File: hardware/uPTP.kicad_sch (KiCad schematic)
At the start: 24 parts, among them J1 UART_HDR, J2 PPS_UFL, J3 PPS_SMA, J5 AUX_PWR, J6 PROG, U1 CH32V307WCU6, X1 X50328MSB2GI

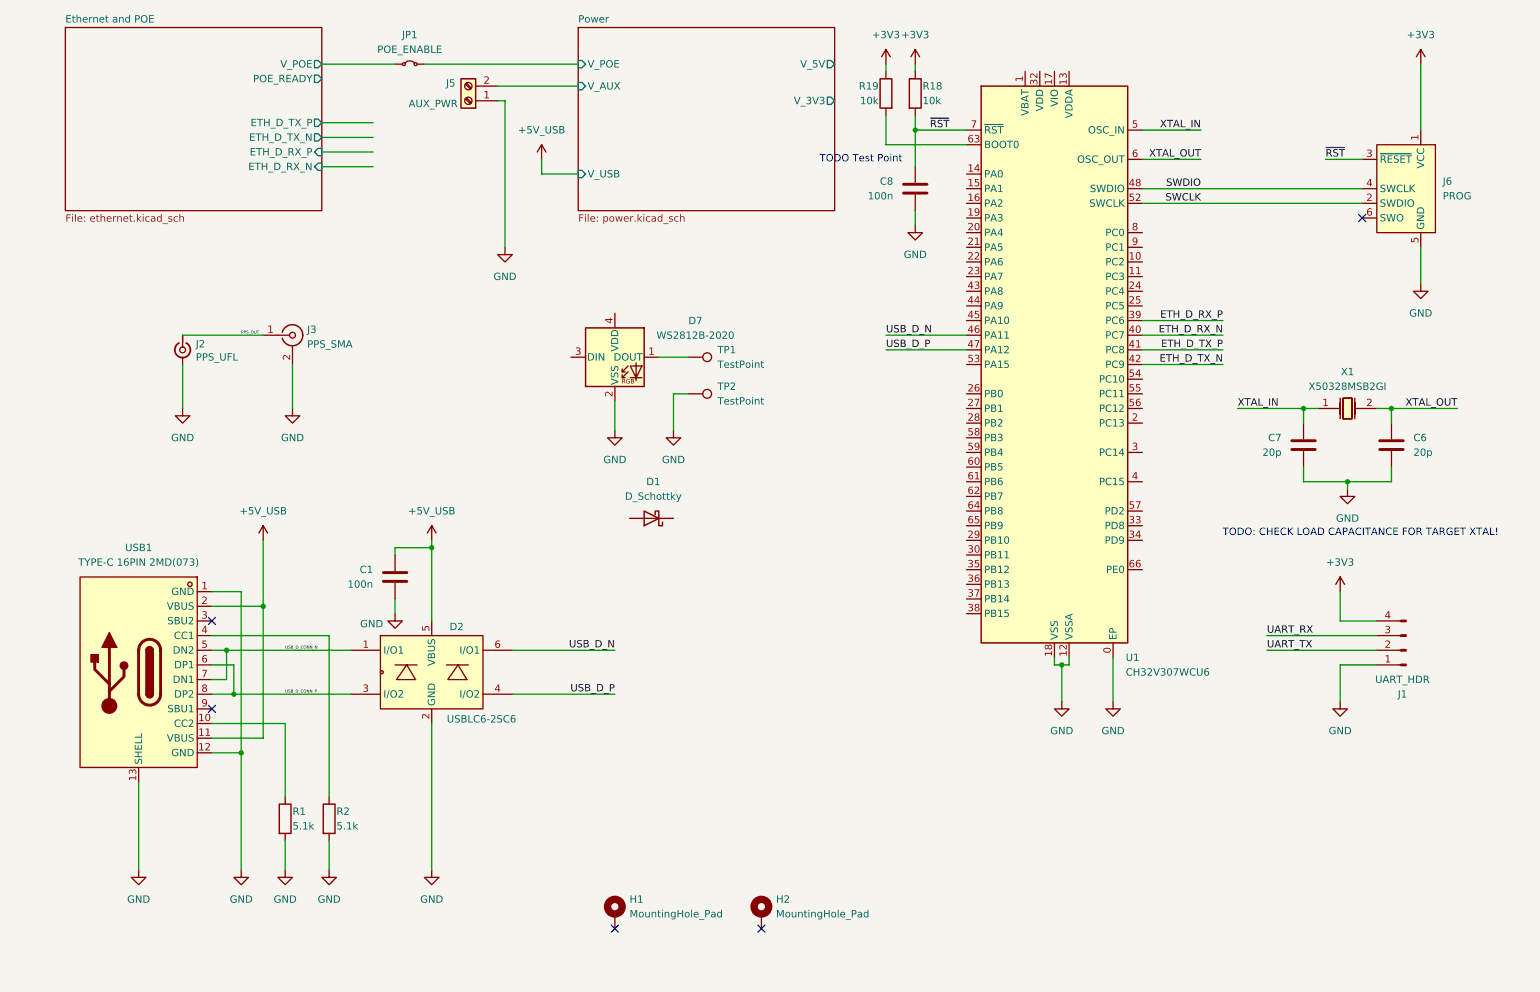
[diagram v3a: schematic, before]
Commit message: Neaten up schematic hierarchy
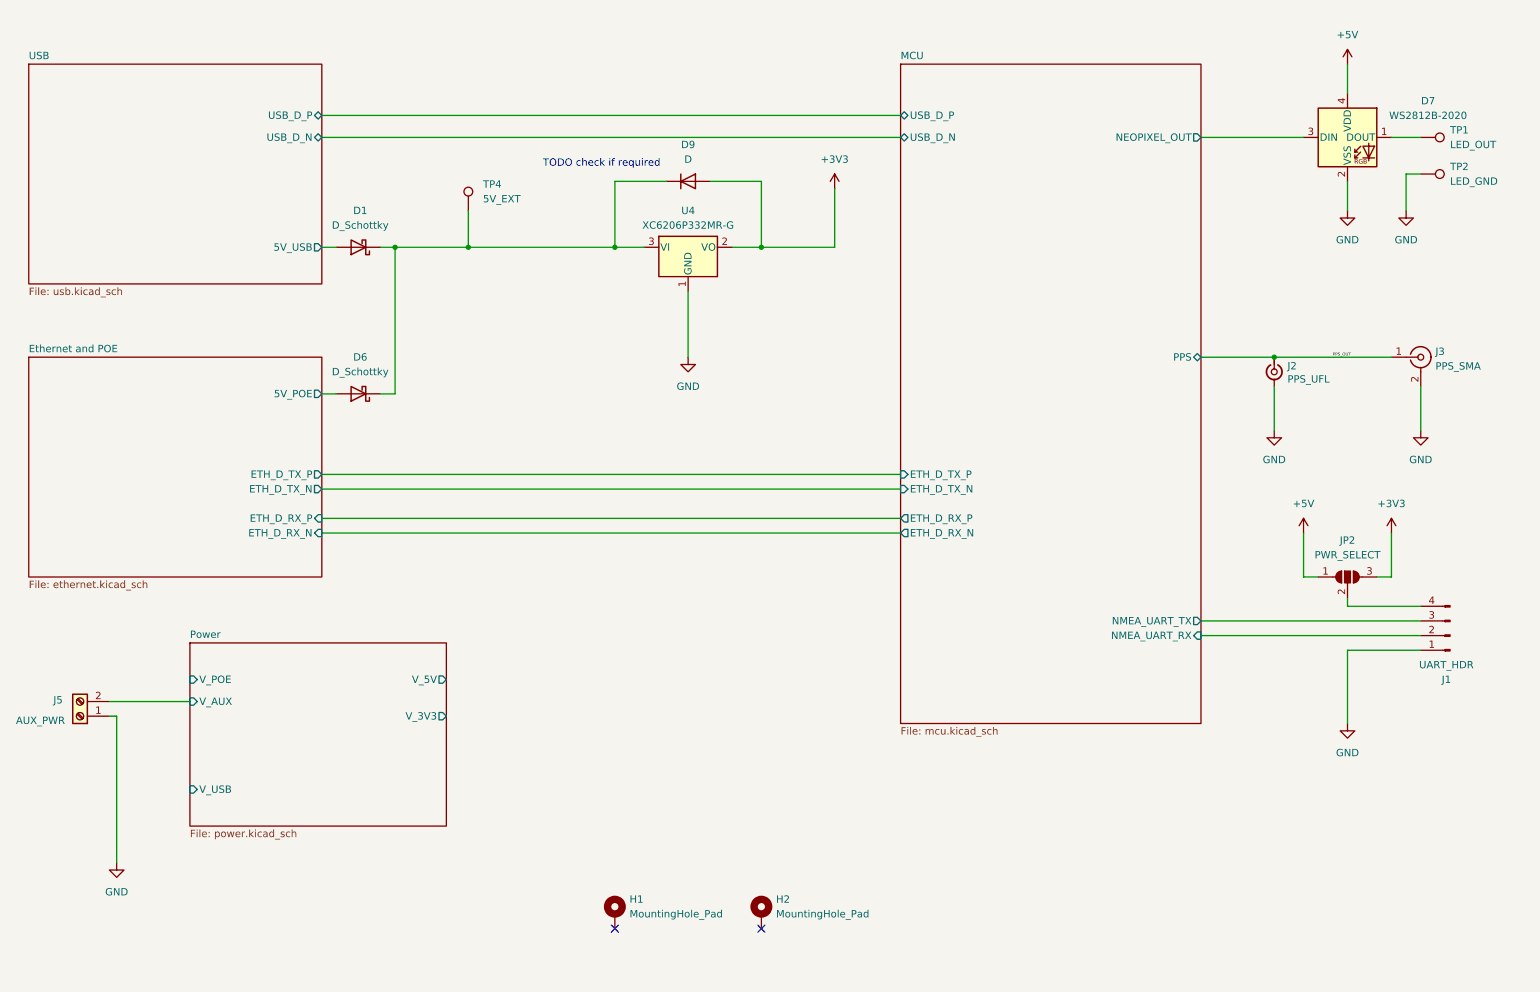
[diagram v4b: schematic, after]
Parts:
- removed C1, C8: 100n, Capacitor_SMD:C_0402_1005Metric, symbol Device:C
- removed C6, C7: 20p, Capacitor_SMD:C_0402_1005Metric, symbol Device:C
- removed D2: USBLC6-2SC6, uPTP:SOT-23-6_L2.9-W1.6-P0.95-LS2.8-BL, symbol uPTP:USBLC6-2SC6
- removed J6: PROG, Connector:Tag-Connect_TC2030-IDC-NL_2x03_P1.27mm_Vertical, symbol Connector:Conn_ARM_SWD_TagConnect_TC2030-NL
- removed JP1: POE_ENABLE, Jumper:SolderJumper-2_P1.3mm_Bridged_RoundedPad1.0x1.5mm, symbol Jumper:Jumper_2_Small_Bridged
- removed R1, R2: 5.1k, Resistor_SMD:R_0402_1005Metric, symbol Device:R
- removed R18, R19: 10k, Resistor_SMD:R_0402_1005Metric, symbol Device:R
- removed U1: CH32V307WCU6, uPTP:QFN-68_L8.0-W8.0-P0.40-BL-EP6.7, symbol uPTP:CH32V30xWxUx
- removed USB1: TYPE-C 16PIN 2MD(073), uPTP:USB-C-SMD_TYPE-C-16PIN, symbol uPTP:USB-C-SMD_TYPE-C-16PIN
- removed X1: X50328MSB2GI, uPTP:CRYSTAL-SMD_L5.0-W3.2, symbol uPTP:X50328MSB2GI
- added D6: D_Schottky, Diode_SMD:D_SOD-323, symbol Device:D_Schottky
- added D9: D, symbol Device:D
- added JP2: PWR_SELECT, symbol Jumper:SolderJumper_3_Open
- added TP4: 5V_EXT, symbol Connector:TestPoint
- added U4: XC6206P332MR-G, Package_TO_SOT_SMD:SOT-23-3, symbol Regulator_Linear:XC6206PxxxMR
- TP1: value TestPoint -> LED_OUT
- TP2: value TestPoint -> LED_GND
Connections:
- net +3V3: now also D9.2 (A), JP2.3 (B), U4.2 (VO); no longer J1.4 (Pin_4)
- net GND: now also U4.1 (GND)
- net at D1.1 (K): now also D6.1 (K), D9.1 (K), TP4.1, U4.3 (VI)
- net USB/5V_USB: now reaches D1.2 (A)
- net MCU/NEOPIXEL_OUT: now reaches D7.3 (DIN)
- net +5V: now reaches D7.4 (VDD)
- net +5V: now also JP2.1 (A)
- net UART_RX renamed MCU/NMEA_UART_TX
- net UART_TX renamed MCU/NMEA_UART_RX
- new net: J1.4 (Pin_4), JP2.2 (C)
- new net Ethernet and POE/5V_POE: D6.2 (A)
- no-connect marks 5 -> 2
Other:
- added sheet MCU (mcu.kicad_sch)
- added sheet USB (usb.kicad_sch)
- sheet Ethernet and POE ports: added 5V_POE; removed POE_READY, V_POE
- note added: "TODO check if required"
- note removed: "TODO Test Point"
- note removed: "TODO: CHECK LOAD CAPACITANCE FOR TARGET XTAL!"
- moved on the sheet: D1, D7, J1, J2, J3, J5, TP1, TP2

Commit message: Confirm all part footprints, start rought layout
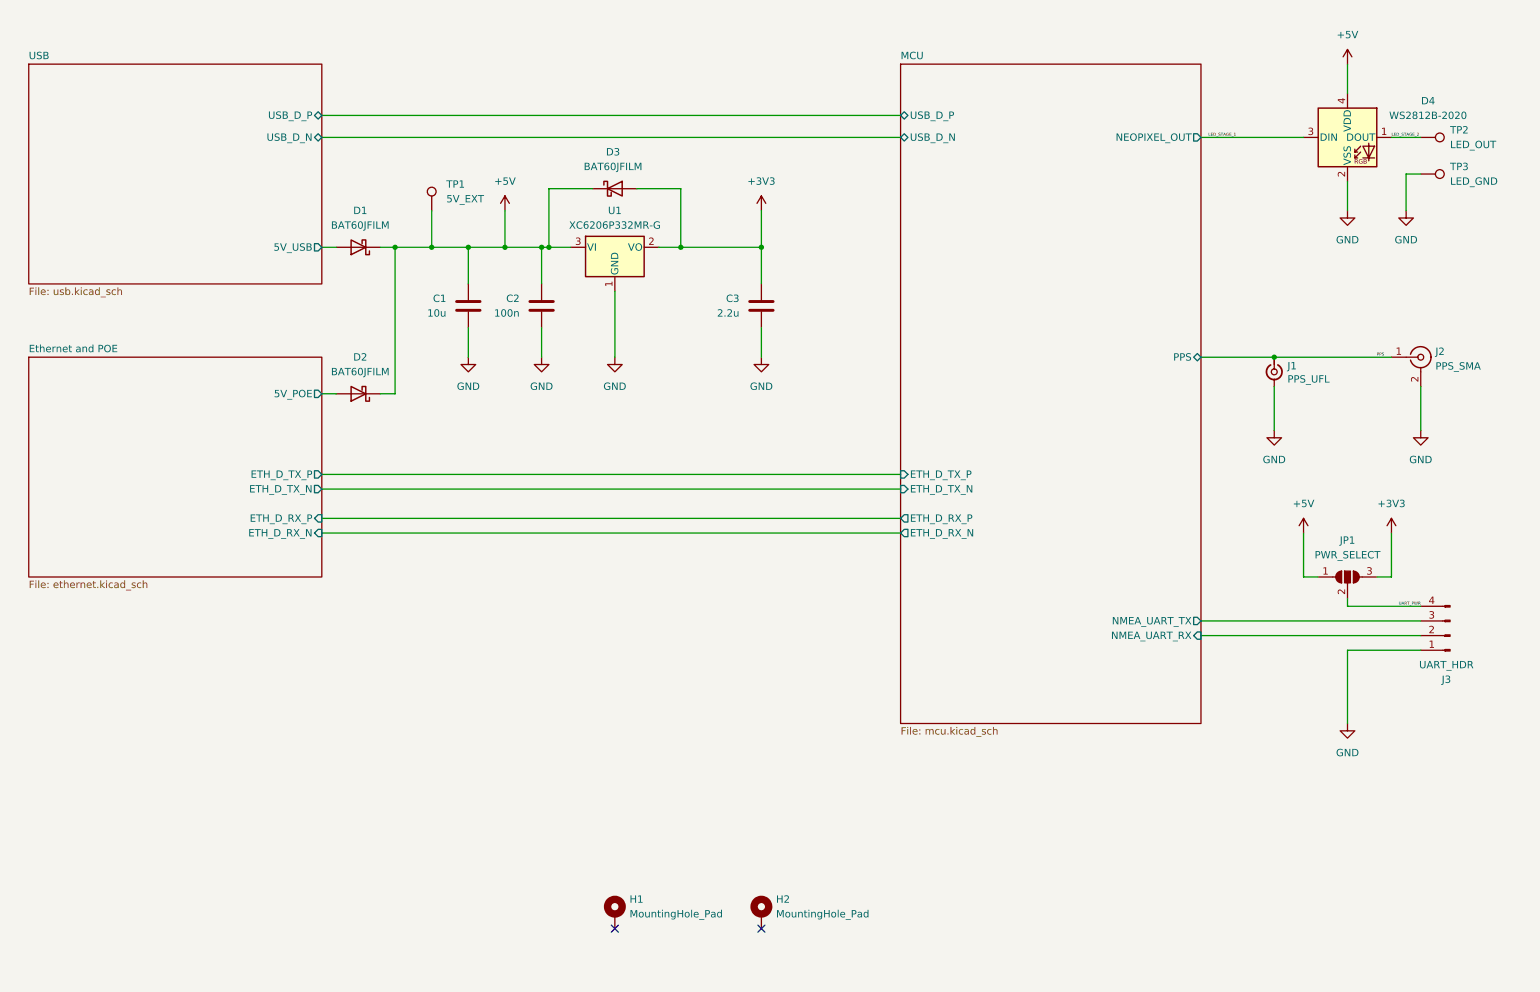
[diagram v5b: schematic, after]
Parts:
- removed D9: D, symbol Device:D
- removed J5: AUX_PWR, TerminalBlock_Phoenix:TerminalBlock_Phoenix_MPT-0,5-2-2.54_1x02_P2.54mm_Horizontal, symbol Connector:Screw_Terminal_01x02
- added C1: 10u, Capacitor_SMD:C_0603_1608Metric, symbol Device:C
- added C2: 100n, Capacitor_SMD:C_0402_1005Metric, symbol Device:C
- added C3: 2.2u, Capacitor_SMD:C_0402_1005Metric, symbol Device:C
- added D3: BAT60JFILM, Diode_SMD:D_SOD-323, symbol Device:D_Schottky
- D1: value D_Schottky -> BAT60JFILM
- D2: renamed from D6; value D_Schottky -> BAT60JFILM
- JP1: renamed from JP2; footprint (none) -> Jumper:SolderJumper-3_P1.3mm_Open_RoundedPad1.0x1.5mm_NumberLabels
- TP1: renamed from TP4; footprint (none) -> TestPoint:TestPoint_Pad_D1.5mm
- TP2: renamed from TP1; footprint (none) -> TestPoint:TestPoint_Pad_D1.5mm
- TP3: renamed from TP2; footprint (none) -> TestPoint:TestPoint_Pad_D1.5mm
- renumbered D7 to D4, J2 to J1, J3 to J2, J1 to J3, U4 to U1
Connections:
- net +3V3: now also C3.1, D3.2 (A)
- net +5V: now also D1.1 (K), D2.1 (K), TP1.1, U1.3 (VI), C1.1, C2.1, D3.1 (K)
- net GND: now also C1.2, C2.2, C3.2
- net UART_PWR: now reaches J3.4 (Pin_4), JP1.2 (C)
- net LED_STAGE_2: now reaches D4.1 (DOUT), TP2.1
- net MCU/NEOPIXEL_OUT renamed LED_STAGE_1
- net PPS_OUT renamed PPS
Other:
- removed sheet Power
- note removed: "TODO check if required"
- moved on the sheet: TP1, U1

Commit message: Tidy up layout
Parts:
- removed TP2: LED_OUT, TestPoint:TestPoint_Pad_D1.5mm, symbol Connector:TestPoint
- removed TP3: LED_GND, TestPoint:TestPoint_Pad_D1.5mm, symbol Connector:TestPoint
- added J3: LED, Connector_PinHeader_1.27mm:PinHeader_1x03_P1.27mm_Vertical, symbol Connector:Conn_01x03_Pin
- renumbered J3 to J4
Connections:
- net +5V: now also J3.3 (Pin_3)
- net GND: now also J3.1 (Pin_1)
- net LED_STAGE_2: now also J3.2 (Pin_2)
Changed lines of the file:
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@@
+	(wire
+		(pts
+			(xy 264.16 53.34) (xy 266.7 53.34)
+		)
+		(stroke
+			(width 0)
+			(type default)
+		)
+	)
+	(wire
+		(pts
+			(xy 264.16 48.26) (xy 266.7 48.26)
+		)
+		(stroke
+			(width 0)
+			(type default)
+		)
+	)
 	(wire
 		(pts
@@
 	(wire
 		(pts
-			(xy 264.16 57.15) (xy 266.7 57.15)
-		)
-		(stroke
-			(width 0)
-			(type default)
-		)
-	)
-	(wire
-		(pts
 			(xy 101.6 69.85) (xy 107.95 69.85)
 		)
@@
 	(wire
 		(pts
+			(xy 264.16 38.1) (xy 264.16 48.26)
+		)
+		(stroke
+			(width 0)
+			(type default)
+		)
+	)
+	(wire
+		(pts
 			(xy 76.2 116.84) (xy 176.53 116.84)
 		)
@@
 	(wire
 		(pts
-			(xy 264.16 57.15) (xy 264.16 63.5)
+			(xy 264.16 53.34) (xy 264.16 63.5)
 		)
 		(stroke
@@
 	)
 	(symbol
-		(lib_id "Connector:TestPoint")
-		(at 266.7 57.15 270)
-		(unit 1)
-		(exclude_from_sim no)
-		(in_bom yes)
-		(on_board yes)
-		(dnp no)
-		(fields_autoplaced yes)
-		(property "Reference" "TP3"
-			(at 271.78 55.8799 90)
-			(effects
-				(font
-					(size 1.27 1.27)
-				)
-				(justify left)
-			)
-		)
-		(property "Value" "LED_GND"
-			(at 271.78 58.4199 90)
-			(effects
-				(font
-					(size 1.27 1.27)
-				)
-				(justify left)
-			)
-		)
-		(property "Footprint" "TestPoint:TestPoint_Pad_D1.5mm"
-			(at 266.7 62.23 0)
-			(effects
-				(font
-					(size 1.27 1.27)
-				)
-				(hide yes)
-			)
-		)
-		(property "Datasheet" "~"
-			(at 266.7 62.23 0)
-			(effects
-				(font
-					(size 1.27 1.27)
-				)
-				(hide yes)
-			)
-		)
-		(property "Description" "test point"
-			(at 266.7 57.15 0)
-			(effects
-				(font
-					(size 1.27 1.27)
-				)
-				(hide yes)
-			)
-		)
-		(pin "1"
-		)
-		(instances
-			(project "uPTP"
-				(path "/c29659fd-9e8d-4714-a690-4e74e6e849c2"
-					(reference "TP3")
-					(unit 1)
-				)
-			)
-		)
-	)
-	(symbol
 		(lib_id "Mechanical:MountingHole_Pad")
 		(at 152.4 185.42 0)
@@
 	)
 	(symbol
+		(lib_id "Connector:Conn_01x03_Pin")
+		(at 271.78 50.8 180)
+		(unit 1)
+		(exclude_from_sim no)
+		(in_bom yes)
+		(on_board yes)
+		(dnp no)
+		(fields_autoplaced yes)
+		(property "Reference" "J3"
+			(at 273.05 49.5299 0)
+			(effects
+				(font
+					(size 1.27 1.27)
+				)
+				(justify right)
+			)
+		)
+		(property "Value" "LED"
+			(at 273.05 52.0699 0)
+			(effects
+				(font
+					(size 1.27 1.27)
+				)
+				(justify right)
+			)
+		)
+		(property "Footprint" "Connector_PinHeader_1.27mm:PinHeader_1x03_P1.27mm_Vertical"
+			(at 271.78 50.8 0)
+			(effects
+				(font
+					(size 1.27 1.27)
+				)
+				(hide yes)
+			)
+		)
+		(property "Datasheet" "~"
+			(at 271.78 50.8 0)
+			(effects
+				(font
+					(size 1.27 1.27)
+				)
+				(hide yes)
+			)
+		)
+		(property "Description" "Generic connector, single row, 01x03, script generated"
+			(at 271.78 50.8 0)
+			(effects
+				(font
+					(size 1.27 1.27)
+				)
+				(hide yes)
+			)
+		)
+		(pin "1"
+		)
+		(pin "2"
+		)
+		(pin "3"
+		)
+		(instances
+			(project ""
+				(path "/c29659fd-9e8d-4714-a690-4e74e6e849c2"
+					(reference "J3")
+					(unit 1)
+				)
+			)
+		)
+	)
+	(symbol
 		(lib_id "Device:D_Schottky")
 		(at 82.55 95.25 180)
@@
 		(on_board yes)
 		(dnp no)
-		(fields_autoplaced yes)
 		(property "Reference" "D4"
-			(at 267.97 44.4814 0)
+			(at 250.19 43.942 0)
 			(effects
 				(font
@@
 		)
 		(property "Value" "WS2812B-2020"
-			(at 267.97 47.0214 0)
+			(at 244.094 57.658 0)
 			(effects
 				(font
@@
 		(dnp no)
 		(fields_autoplaced yes)
-		(property "Reference" "#PWR013"
+		(property "Reference" "#PWR014"
 			(at 264.16 69.85 0)
 			(effects
@@
 			(project "uPTP"
 				(path "/c29659fd-9e8d-4714-a690-4e74e6e849c2"
+					(reference "#PWR014")
+					(unit 1)
+				)
+			)
+		)
+	)
+	(symbol
+		(lib_id "power:+5V")
+		(at 264.16 38.1 0)
+		(unit 1)
+		(exclude_from_sim no)
+		(in_bom yes)
+		(on_board yes)
+		(dnp no)
+		(fields_autoplaced yes)
+		(property "Reference" "#PWR013"
+			(at 264.16 41.91 0)
+			(effects
+				(font
+					(size 1.27 1.27)
+				)
+				(hide yes)
+			)
+		)
+		(property "Value" "+5V"
+			(at 264.16 33.02 0)
+			(effects
+				(font
+					(size 1.27 1.27)
+				)
+			)
+		)
+		(property "Footprint" ""
+			(at 264.16 38.1 0)
+			(effects
+				(font
+					(size 1.27 1.27)
+				)
+				(hide yes)
+			)
+		)
+		(property "Datasheet" ""
+			(at 264.16 38.1 0)
+			(effects
+				(font
+					(size 1.27 1.27)
+				)
+				(hide yes)
+			)
+		)
+		(property "Description" "Power symbol creates a global label with name \"+5V\""
+			(at 264.16 38.1 0)
+			(effects
+				(font
+					(size 1.27 1.27)
+				)
+				(hide yes)
+			)
+		)
+		(pin "1"
+		)
+		(instances
+			(project "uPTP"
+				(path "/c29659fd-9e8d-4714-a690-4e74e6e849c2"
 					(reference "#PWR013")
-					(unit 1)
-				)
-			)
-		)
-	)
-	(symbol
-		(lib_id "Connector:TestPoint")
-		(at 266.7 50.8 270)
-		(unit 1)
-		(exclude_from_sim no)
-		(in_bom yes)
-		(on_board yes)
-		(dnp no)
-		(fields_autoplaced yes)
-		(property "Reference" "TP2"
-			(at 271.78 49.5299 90)
-			(effects
-				(font
-					(size 1.27 1.27)
-				)
-				(justify left)
-			)
-		)
-		(property "Value" "LED_OUT"
-			(at 271.78 52.0699 90)
-			(effects
-				(font
-					(size 1.27 1.27)
-				)
-				(justify left)
-			)
-		)
-		(property "Footprint" "TestPoint:TestPoint_Pad_D1.5mm"
-			(at 266.7 55.88 0)
-			(effects
-				(font
-					(size 1.27 1.27)
-				)
-				(hide yes)
-			)
-		)
-		(property "Datasheet" "~"
-			(at 266.7 55.88 0)
-			(effects
-				(font
-					(size 1.27 1.27)
-				)
-				(hide yes)
-			)
-		)
-		(property "Description" "test point"
-			(at 266.7 50.8 0)
-			(effects
-				(font
-					(size 1.27 1.27)
-				)
-				(hide yes)
-			)
-		)
-		(pin "1"
-		)
-		(instances
-			(project ""
-				(path "/c29659fd-9e8d-4714-a690-4e74e6e849c2"
-					(reference "TP2")
 					(unit 1)
 				)
@@
 		(on_board yes)
 		(dnp no)
-		(property "Reference" "J3"
+		(property "Reference" "J4"
 			(at 271.145 144.78 0)
 			(effects
@@
 			(project ""
 				(path "/c29659fd-9e8d-4714-a690-4e74e6e849c2"
-					(reference "J3")
+					(reference "J4")
 					(unit 1)
 				)
@@
 		(dnp no)
 		(fields_autoplaced yes)
-		(property "Reference" "#PWR014"
+		(property "Reference" "#PWR015"
 			(at 266.7 107.95 0)
 			(effects
@@
 			(project ""
 				(path "/c29659fd-9e8d-4714-a690-4e74e6e849c2"
-					(reference "#PWR014")
-					(unit 1)
-				)
+					(reference "#PWR015")
+					(unit 1)
+				)
